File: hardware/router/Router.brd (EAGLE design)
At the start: 133.3 x 101.6 mm, 53 parts, among them J1 AVR_PROG, J10 RJ45-8PTH, J11 RJ45-8PTH, J12 RJ45-8PTH, J13 RJ45-8PTH, J14 RJ45-8PTH, J15 RJ45-8PTH, J16 RJ45-8PTH, J17 RASPBERRYPI_BB, J18 RJ45-8PTH, J19 RJ45-8PTH, J2 RJ45-8PTH, J3 RJ45-8PTH, J4 RJ45-8PTH, J5 RJ45-8PTH, J6 RJ45-8PTH, J7 RJ45-8PTH, J8 RJ45-8PTH, J9 RJ45-8PTH, Q1 NMOS, Q2 NMOS, Q3 NMOS, U1 ATMEGA168, U3 DS1307SO8, U6 CON-MATENLOK, Y1 32.768kHz

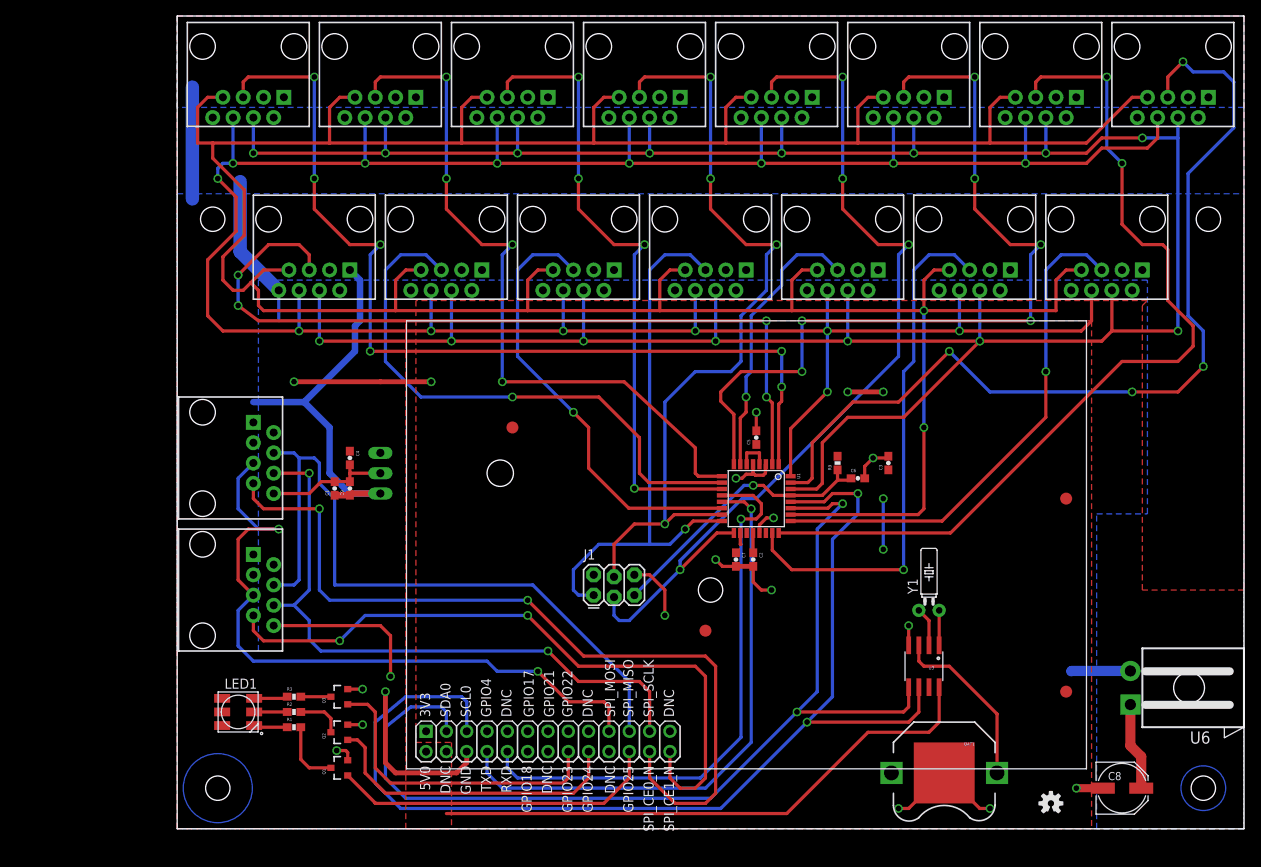
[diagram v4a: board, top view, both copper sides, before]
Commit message: Final files that were used to CAM dispenser and router boards
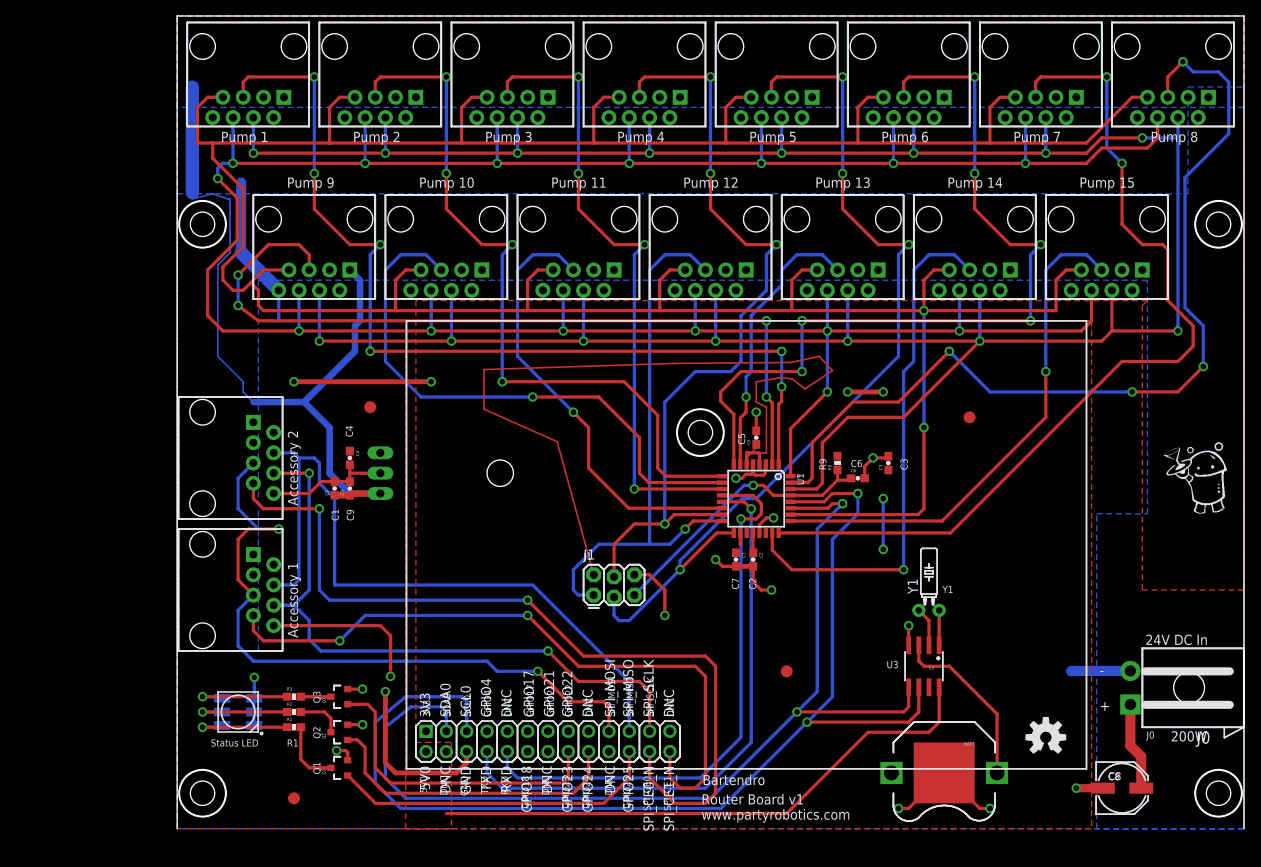
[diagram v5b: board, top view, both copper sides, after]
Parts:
- removed FRAME3: FRAME-LETTER, SparkFun-Aesthetics:CREATIVE_COMMONS
- removed U$5: OSHW-LOGOS, SparkFun-Aesthetics:OSHW-LOGO-S
- added U$46: OSHW-LOGOM, SparkFun-Aesthetics:OSHW-LOGO-M
- moved JP2 97.4 mm to (14.6, 3.81)
- moved JP9 19.7 mm to (65.4, 49.5)
- moved JP3 18.0 mm to (24.1, 52.7)
- moved JP1 15.8 mm to (99.1, 51.4)
- moved JP4 11.4 mm to (76.2, 19.7)
- moved JP7 2.01 mm to (130.2, 4.45)
- moved JP6 2.01 mm to (3.17, 4.45)
- moved JP8 1.42 mm to (130.2, 75.6)
- moved JP5 1.42 mm to (3.17, 75.6)
- flipped LED1 to the bottom
- renumbered U6 to J0
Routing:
- net 3.3V: track 12.3 -> 116.5 mm
- net VIN: track 74.7 -> 107.4 mm
- net N$9: track 4.22 -> 13.1 mm, vias 0 -> 1
- net N$13: track 4.22 -> 13.1 mm, vias 0 -> 1
- net N$12: track 4.14 -> 13.0 mm, vias 0 -> 1
- net 5V: track 70.7 -> 76.7 mm, vias 0 -> 1
- net RX3: track 89.4 -> 91.6 mm
- net RX0: track 115.8 -> 115.2 mm
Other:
- outline, holes or cut-outs redrawn
- board text added: "+"
- board text added: "-"
- board text added: "200W"
- board text added: "24V DC In"
- board text added: "3V3"
- board text added: "5V0"
- board text added: "Accessory 1"
- board text added: "Accessory 2"
- board text added: "Bartendro"
- board text added: "C1"
- board text added: "C2"
- board text added: "C3"
- board text added: "C4"
- board text added: "C5"
- board text added: "C6"
- board text added: "C7"
- board text added: "C8"
- board text added: "C9"
- board text added: "DNC"
- board text added: "GND"
- board text added: "GPIO17"
- board text added: "GPIO18"
- board text added: "GPIO21"
- board text added: "GPIO22"
- board text added: "GPIO23"
- board text added: "GPIO24"
- board text added: "GPIO25"
- board text added: "GPIO4"
- board text added: "J0"
- board text added: "J1"
- board text added: "Pump 1"
- board text added: "Pump 10"
- board text added: "Pump 11"
- board text added: "Pump 12"
- board text added: "Pump 13"
- board text added: "Pump 14"
- board text added: "Pump 15"
- board text added: "Pump 2"
- board text added: "Pump 3"
- board text added: "Pump 4"
- board text added: "Pump 5"
- board text added: "Pump 6"
- board text added: "Pump 7"
- board text added: "Pump 8"
- board text added: "Pump 9"
- board text added: "Q1"
- board text added: "Q2"
- board text added: "Q3"
- board text added: "R1"
- board text added: "R9"
- board text added: "RXD"
- board text added: "Router Board v1"
- board text added: "SCL0"
- board text added: "SDA0"
- board text added: "SPI_CE0"
- board text added: "SPI_CE1"
- board text added: "SPI_MISO"
- board text added: "SPI_MOSI"
- board text added: "SPI_SCLK"
- board text added: "Status LED"
- board text added: "TXD"
- board text added: "U1"
- board text added: "U2"
- board text added: "U3"
- board text added: "Y1"
- board text added: "www.partyrobotics.com"

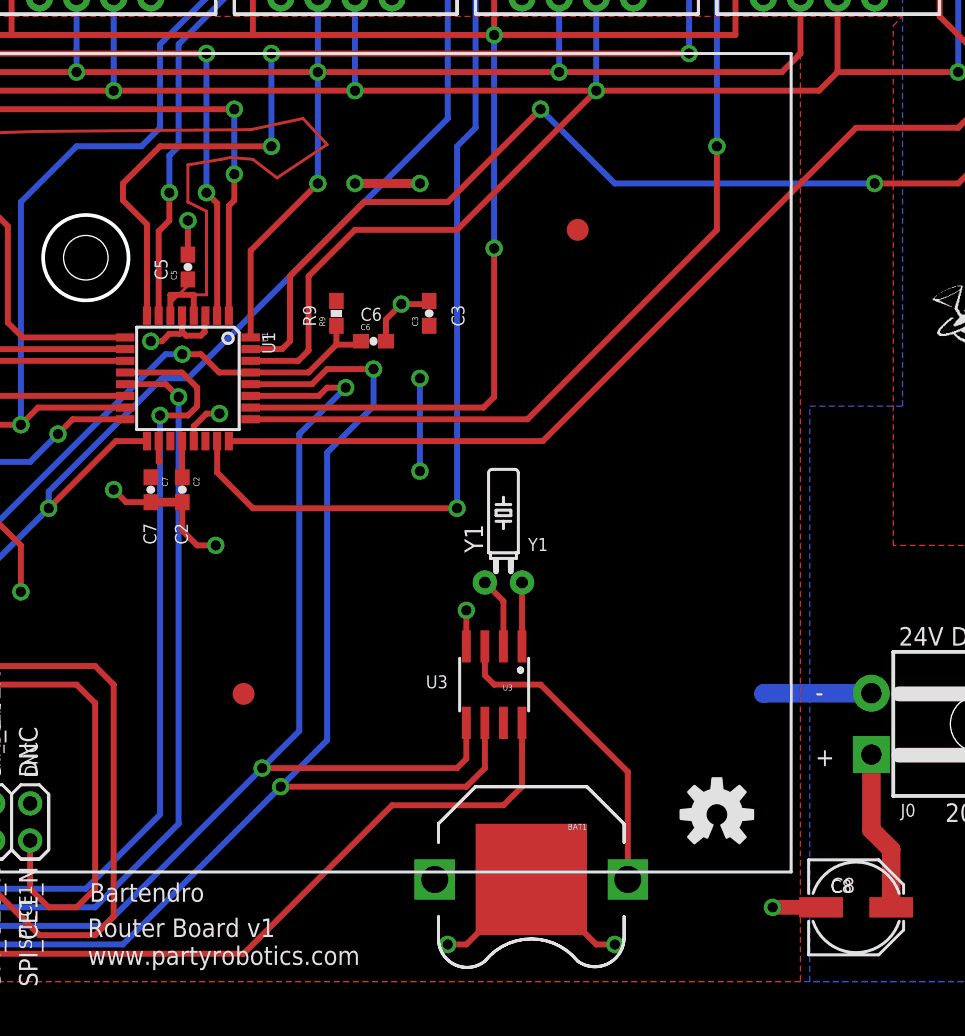
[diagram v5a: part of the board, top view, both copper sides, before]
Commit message: Updated to schematic and layout to Rev 1.1 (PD0 and PD1 swapped)
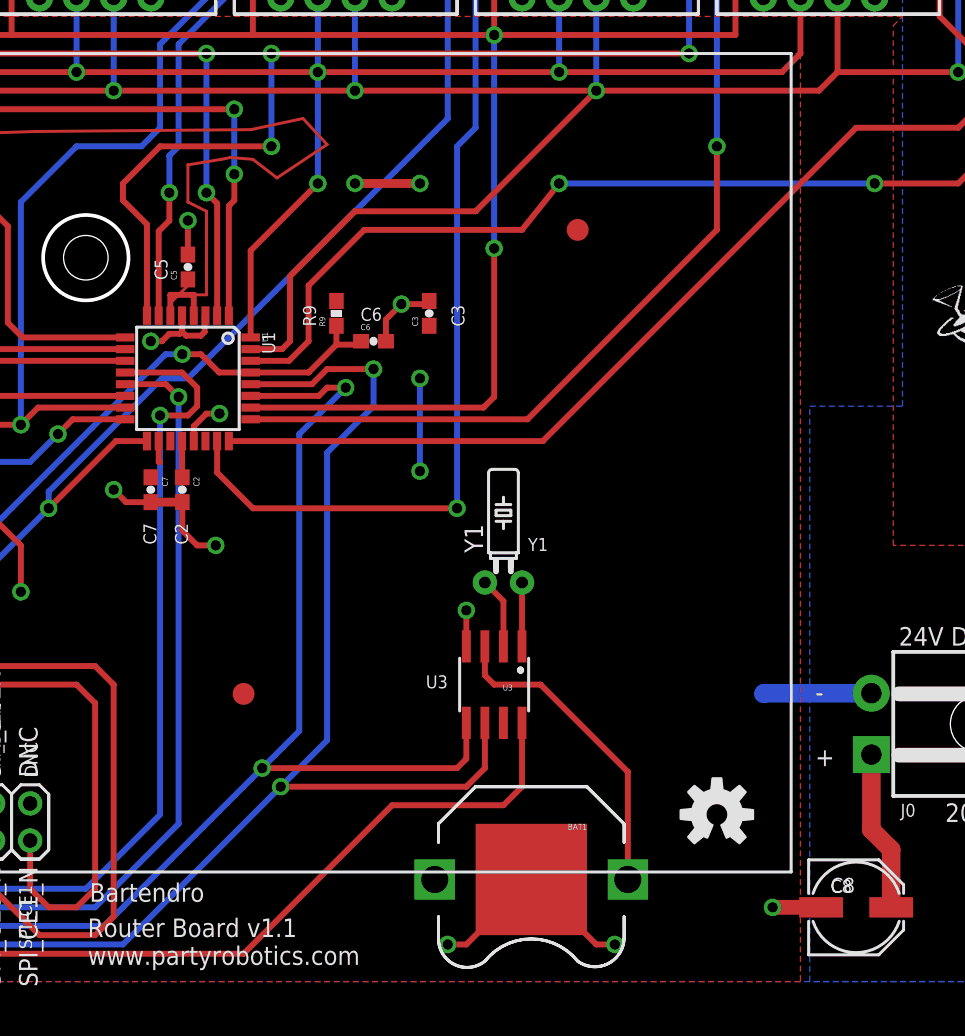
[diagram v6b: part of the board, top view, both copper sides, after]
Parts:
- added FRAME3: FRAME-LETTER, SparkFun-Aesthetics:CREATIVE_COMMONS
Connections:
- net RX0: now also U1.30; no longer U1.31
- net TX: now also U1.31; no longer U1.30
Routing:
- net RX0: track 115.2 -> 111.1 mm
- net TX: track 359.4 -> 358.7 mm
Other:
- board text added: "Router Board v1.1"
- board text removed: "Router Board v1"
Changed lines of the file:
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@@
 <text x="65.532" y="1.143" size="1.27" layer="121" font="vector" ratio="16">www.partyrobotics.com</text>
 <text x="65.659" y="5.461" size="1.27" layer="121" font="vector" ratio="16">Bartendro</text>
-<text x="65.532" y="3.048" size="1.27" layer="121" font="vector" ratio="16">Router Board v1</text>
+<text x="65.532" y="3.048" size="1.27" layer="121" font="vector" ratio="16">Router Board v1.1</text>
 </plain>
 <attributes>
@@
 <element name="J17" library="pierre" package="RASBERRYPI_SHIELD" value="RASPBERRYPI_BB" x="28.575" y="7.62"/>
 <element name="U$46" library="SparkFun-Aesthetics" package="OSHW-LOGO-M" value="OSHW-LOGOM" x="108.585" y="11.43"/>
+<element name="FRAME3" library="SparkFun-Aesthetics" package="CREATIVE_COMMONS" value="FRAME-LETTER" x="19.05" y="-10.16"/>
 </elements>
 <signals>
@@
 <signal name="RX0">
 <contactref element="J9" pad="5"/>
-<contactref element="U1" pad="31"/>
 <wire x1="131.445" y1="86.868" x2="125.984" y2="81.407" width="0.4064" layer="16"/>
 <wire x1="125.984" y1="81.407" x2="125.984" y2="65.151" width="0.4064" layer="16"/>
@@
 <wire x1="130.175" y1="94.615" x2="131.445" y2="93.345" width="0.4064" layer="16"/>
 <wire x1="131.445" y1="93.345" x2="131.445" y2="86.868" width="0.4064" layer="16"/>
-<wire x1="76.6826" y1="43.275" x2="78.835" y2="43.275" width="0.4064" layer="1"/>
-<wire x1="78.835" y1="43.275" x2="79.375" y2="43.815" width="0.4064" layer="1"/>
-<wire x1="79.375" y1="43.815" x2="79.375" y2="48.26" width="0.4064" layer="1"/>
-<wire x1="79.375" y1="48.26" x2="84.455" y2="53.34" width="0.4064" layer="1"/>
+<wire x1="79.305" y1="42.475" x2="80.645" y2="43.815" width="0.4064" layer="1"/>
+<wire x1="80.645" y1="43.815" x2="80.645" y2="47.625" width="0.4064" layer="1"/>
+<wire x1="80.645" y1="47.625" x2="84.455" y2="51.435" width="0.4064" layer="1"/>
 <wire x1="125.984" y1="65.151" x2="128.27" y2="62.865" width="0.4064" layer="16"/>
 <wire x1="128.27" y1="62.865" x2="128.27" y2="57.785" width="0.4064" layer="16"/>
 <via x="128.27" y="57.785" extent="1-16" drill="0.7"/>
-<wire x1="84.455" y1="53.34" x2="90.17" y2="53.34" width="0.4064" layer="1"/>
-<wire x1="90.17" y1="53.34" x2="96.52" y2="59.69" width="0.4064" layer="1"/>
-<via x="96.52" y="59.69" extent="1-16" drill="0.7"/>
-<wire x1="96.52" y1="59.69" x2="101.6" y2="54.61" width="0.4064" layer="16"/>
-<wire x1="101.6" y1="54.61" x2="119.38" y2="54.61" width="0.4064" layer="16"/>
+<wire x1="84.455" y1="51.435" x2="95.25" y2="51.435" width="0.4064" layer="1"/>
+<wire x1="95.25" y1="51.435" x2="97.79" y2="54.61" width="0.4064" layer="1"/>
+<via x="97.79" y="54.61" extent="1-16" drill="0.7"/>
+<wire x1="97.79" y1="54.61" x2="119.38" y2="54.61" width="0.4064" layer="16"/>
 <via x="119.38" y="54.61" extent="1-16" drill="0.7"/>
 <wire x1="128.27" y1="57.785" x2="125.095" y2="54.61" width="0.4064" layer="1"/>
 <wire x1="125.095" y1="54.61" x2="119.38" y2="54.61" width="0.4064" layer="1"/>
+<contactref element="U1" pad="30"/>
+<wire x1="76.6826" y1="42.475" x2="79.305" y2="42.475" width="0.4064" layer="1"/>
 </signal>
 <signal name="RX1">
@@
 <signal name="TX">
 <contactref element="J9" pad="4"/>
-<contactref element="U1" pad="30"/>
 <contactref element="J2" pad="4"/>
 <contactref element="J10" pad="4"/>
@@
 <wire x1="115.57" y1="60.96" x2="116.84" y2="62.23" width="0.4064" layer="1"/>
 <wire x1="116.84" y1="62.23" x2="116.84" y2="67.31" width="0.4064" layer="1"/>
-<wire x1="76.6826" y1="42.475" x2="79.94" y2="42.475" width="0.4064" layer="1"/>
-<wire x1="79.94" y1="42.475" x2="80.645" y2="43.18" width="0.4064" layer="1"/>
-<wire x1="80.645" y1="43.18" x2="80.645" y2="48.26" width="0.4064" layer="1"/>
-<wire x1="80.645" y1="48.26" x2="83.82" y2="51.435" width="0.4064" layer="1"/>
-<wire x1="83.82" y1="51.435" x2="90.805" y2="51.435" width="0.4064" layer="1"/>
-<wire x1="90.805" y1="51.435" x2="100.33" y2="60.96" width="0.4064" layer="1"/>
 <wire x1="125.095" y1="62.23" x2="116.84" y2="62.23" width="0.4064" layer="1"/>
 <wire x1="125.095" y1="88.9" x2="125.095" y2="86.36" width="0.4064" layer="16"/>
@@
 <via x="120.65" y="86.36" extent="1-16" drill="0.7"/>
 <wire x1="120.65" y1="86.36" x2="125.095" y2="86.36" width="0.4064" layer="16"/>
+<contactref element="U1" pad="31"/>
+<wire x1="76.6826" y1="43.275" x2="78.835" y2="43.275" width="0.4064" layer="1"/>
+<wire x1="78.835" y1="43.275" x2="79.375" y2="43.815" width="0.4064" layer="1"/>
+<wire x1="79.375" y1="43.815" x2="79.375" y2="48.26" width="0.4064" layer="1"/>
+<wire x1="79.375" y1="48.26" x2="83.82" y2="52.705" width="0.4064" layer="1"/>
+<wire x1="83.82" y1="52.705" x2="92.075" y2="52.705" width="0.4064" layer="1"/>
+<wire x1="92.075" y1="52.705" x2="100.33" y2="60.96" width="0.4064" layer="1"/>
 </signal>
 <signal name="DISP_!RST">
